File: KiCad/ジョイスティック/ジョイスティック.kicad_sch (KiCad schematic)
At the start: 1 part

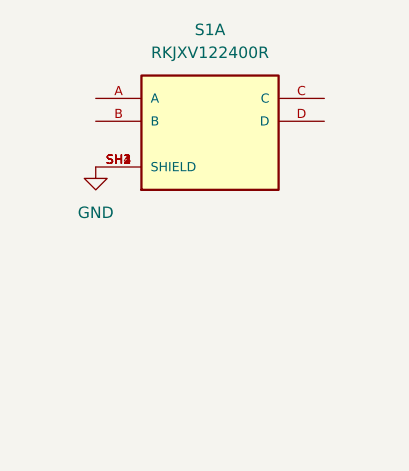
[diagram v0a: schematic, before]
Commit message: wip シールドを介してGNDがつながってる
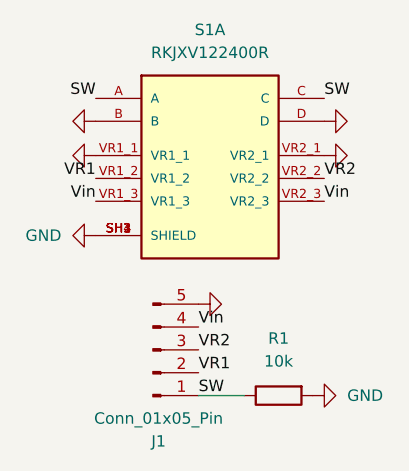
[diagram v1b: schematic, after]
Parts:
- added J1: Conn_01x05_Pin, Connector_PinHeader_2.54mm:PinHeader_1x05_P2.54mm_Horizontal, symbol Connector:Conn_01x05_Pin
- added R1: 10k, Resistor_SMD:R_0603_1608Metric, symbol Device:R
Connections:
- net GND: now also S1.B, S1.D, S1.VR1_1, S1.VR2_1, J1.5 (Pin_5), R1.2
- net SW: now reaches S1.A
- net SW: now also S1.C, J1.1 (Pin_1), R1.1
- new net VR1: J1.2 (Pin_2), S1.VR1_2
- new net VR2: J1.3 (Pin_3), S1.VR2_2
- new net Vin: J1.4 (Pin_4), S1.VR1_3, S1.VR2_3

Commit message: バカの配線を破壊
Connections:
- net GND: no longer R1.2
- net Vin: now also R1.2
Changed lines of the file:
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@@
+		)
+	)
+	(wire
+		(pts
+			(xy 69.85 82.55) (xy 69.85 60.96)
+		)
+		(stroke
+			(width 0)
+			(type default)
+		)
+	)
+	(wire
+		(pts
+			(xy 68.58 82.55) (xy 69.85 82.55)
+		)
+		(stroke
+			(width 0)
+			(type default)
 		)
 	)
@@
 		)
 	)
-	(symbol
-		(lib_id "power:GND")
-		(at 68.58 82.55 90)
-		(unit 1)
-		(exclude_from_sim no)
-		(in_bom yes)
-		(on_board yes)
-		(dnp no)
-		(fields_autoplaced yes)
-		(property "Reference" "#PWR07"
-			(at 74.93 82.55 0)
-			(effects
-				(font
-					(size 1.27 1.27)
-				)
-				(hide yes)
-			)
-		)
-		(property "Value" "GND"
-			(at 72.39 82.5499 90)
-			(effects
-				(font
-					(size 1.27 1.27)
-				)
-				(justify right)
-			)
-		)
-		(property "Footprint" ""
-			(at 68.58 82.55 0)
-			(effects
-				(font
-					(size 1.27 1.27)
-				)
-				(hide yes)
-			)
-		)
-		(property "Datasheet" ""
-			(at 68.58 82.55 0)
-			(effects
-				(font
-					(size 1.27 1.27)
-				)
-				(hide yes)
-			)
-		)
-		(property "Description" "Power symbol creates a global label with name \"GND\" , ground"
-			(at 68.58 82.55 0)
-			(effects
-				(font
-					(size 1.27 1.27)
-				)
-				(hide yes)
-			)
-		)
-		(pin "1"
-		)
-		(instances
-			(project "ジョイスティック"
-				(path "/2795e024-f1e0-4103-aa3b-1bc48db122be"
-					(reference "#PWR07")
-					(unit 1)
-				)
-			)
-		)
-	)
